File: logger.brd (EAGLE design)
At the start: 99 x 44.1 mm, 78 parts, among them IC1 LTC4412, J1 POWER_JACKPTH, Q1 FDN360P, Q2 FDN360P, Q3 2N7002PW, Q4 2N7002PW, U1 DS3231MZ/V+T, U2 FT231X-Q

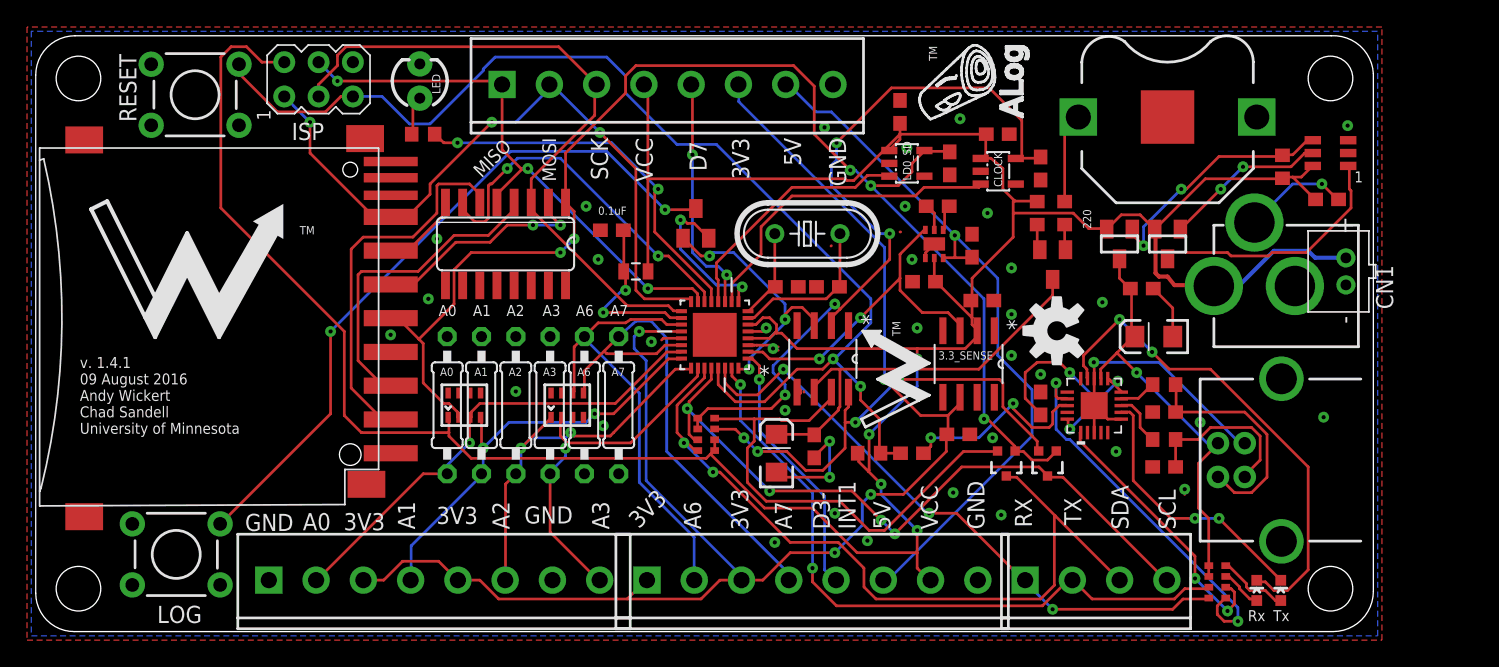
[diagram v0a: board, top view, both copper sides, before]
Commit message: change 3V3 power supply with jumpers, routing needs finishing
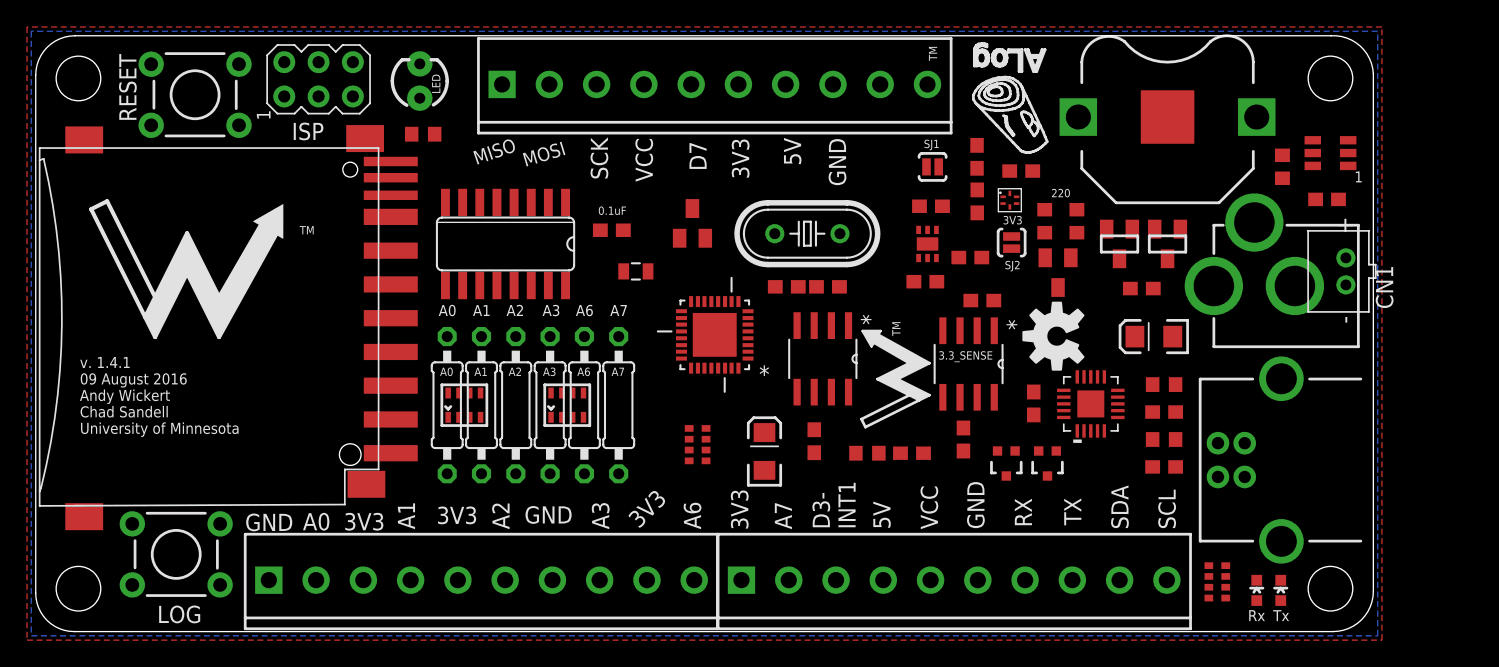
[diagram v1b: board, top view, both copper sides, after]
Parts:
- removed CLOCK, LD0_SD: LP2985, adafruit:SOT23-5L
- removed CLOCK_CIN, SD_CIN: 1uF, rcl:C0603
- removed C_LDO_CLOCK, C_LDO_SD: 2.2uF, resistor:C0603
- removed JP6: (no value), SparkFun-Connectors:SCREWTERMINAL-3.5MM-4
- added 3V3: (no value), csandell:6-TMLF
- added CLOCK_CIN1, CLOCK_CIN2, CLOCK_CIN3: 1uF, rcl:C0603
- added SJ1, SJ2: SOLDERJUMPERNO, SparkFun-Retired:SJ_2S-NO
- 5V_CHARGE_PUMP: value TPS60150 -> 5V5
- D2: value BAT54C -> BAT54
- H0, H1, H3: device SparkFun:SCREWTERMINAL-3.5MM-8 -> SparkFun-Connectors:SCREWTERMINAL-3.5MM-8
- moved H1 7.00 mm to (52.3, 3.81)
- moved U$2 4.47 mm to (72.1, 38.3), turned to 180 degrees
- moved RCLK2 1.09 mm to (77.1, 30.4)
- moved RN2 0.99 mm to (49.0, 13.8)
- moved CLOCK_BATT_DECOUPLE 0.90 mm to (54.0, 13.3)
- moved C_BOOST_3 0.89 mm to (69.2, 27.7), turned to 180 degrees
- moved RCKL1 0.82 mm to (74.7, 30.4)
- moved D1 0.72 mm to (75.7, 26.6)
- moved C_LDO_SENSE 0.54 mm to (68.7, 14.2), turned to 90 degrees
- moved C1 0.51 mm to (73.9, 16.9)
- moved 5V_CHARGE_PUMP 0.50 mm to (66.0, 28.7)
- moved C_BOOST_2 0.50 mm to (66.3, 31.5)
- moved LOGO1 0.40 mm to (75.6, 21.9)
- moved CLOCK_BATT_DECOUP 0.38 mm to (57.7, 14.1)
- moved U2 0.28 mm to (78.1, 16.9)
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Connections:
- removed net D6-CLOCK_3V3_SWITCH: CLOCK.3, MCU.10
- removed net D8-SD_3V3_SWITCH: LD0_SD.3, MCU.12
- new net D6-CLOCK_SD_SWITCH: 3V3.3, MCU.10
- new net D8-EXT: H3.7, MCU.12
- new net N$19: 3V3.4, SJ2.2
- new net N$20: 3V3.1, CLOCK_CIN2.1, SJ1.2
- net +3V3: now also H0.9, H3.8, SJ1.1; no longer H1.3, H3.6
- net 5V: now also H1.4, H3.9; no longer H1.6, H3.7
- net A6: now also H0.10; no longer H1.2
- net A7: now also H1.2; no longer H1.4
- net CLK: now also H3.4; no longer H3.3
- net D3-INT1: now also H1.3; no longer H1.5
- net D4-SENSE_LDO_SWITCH: now also SJ2.1
- net D7-CS-EXT: now also H3.6; no longer H3.5
- net DI: now also H3.2; no longer H3.1
- net DO: now also H3.3; no longer H3.2
- net GND: now also 3V3.5, CLOCK_CIN1.2, CLOCK_CIN2.2, CLOCK_CIN3.2, H1.6, H3.1, H3.10; no longer CLOCK.2, CLOCK_CIN.2, C_LDO_CLOCK.1, C_LDO_SD.1, H1.8, H3.8, LD0_SD.2, SD_CIN.2
- net RX-I: now also H1.7; no longer JP6.1
- net SCL: now also H1.10; no longer JP6.4
- net SDA: now also H1.9; no longer JP6.3
- net TX-O: now also H1.8; no longer JP6.2
- net VCC: now also 3V3.6, CLOCK_CIN1.1, H1.5, H3.5; no longer CLOCK.1, CLOCK_CIN.1, H1.7, H3.4, LD0_SD.1, SD_CIN.1
- net VCL: no longer CLOCK.5, C_LDO_CLOCK.2
- net VDD: now also 3V3.2, CLOCK_CIN3.1; no longer C_LDO_SD.2, LD0_SD.5
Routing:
- net VCC: track 244.3 -> 0.00 mm, vias 4 -> 0
- net +3V3: track 114.1 -> 0.00 mm, vias 4 -> 0
- net VDD: track 99.7 -> 0.00 mm, vias 5 -> 0
- net RESET: track 87.5 -> 0.00 mm, vias 2 -> 0
- net SDA: track 58.2 -> 0.00 mm, vias 2 -> 0
- net VCL: track 56.8 -> 0.00 mm, vias 4 -> 0
- net GND: track 56.5 -> 0.00 mm, vias 38 -> 0
- net 5V: track 53.6 -> 0.00 mm, vias 1 -> 0
- net N$11: track 52.1 -> 0.00 mm, vias 2 -> 0
- net DO: track 52.1 -> 0.00 mm, vias 3 -> 0
- net SCL: track 51.5 -> 0.00 mm, vias 4 -> 0
- net TX-O: track 50.2 -> 0.00 mm, vias 2 -> 0
- net CLK: track 49.8 -> 0.00 mm
- net RX-I: track 46.1 -> 0.00 mm, vias 3 -> 0
- net DI: track 41.9 -> 0.00 mm, vias 3 -> 0
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
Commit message: Routed and ready for Wickert check of approval
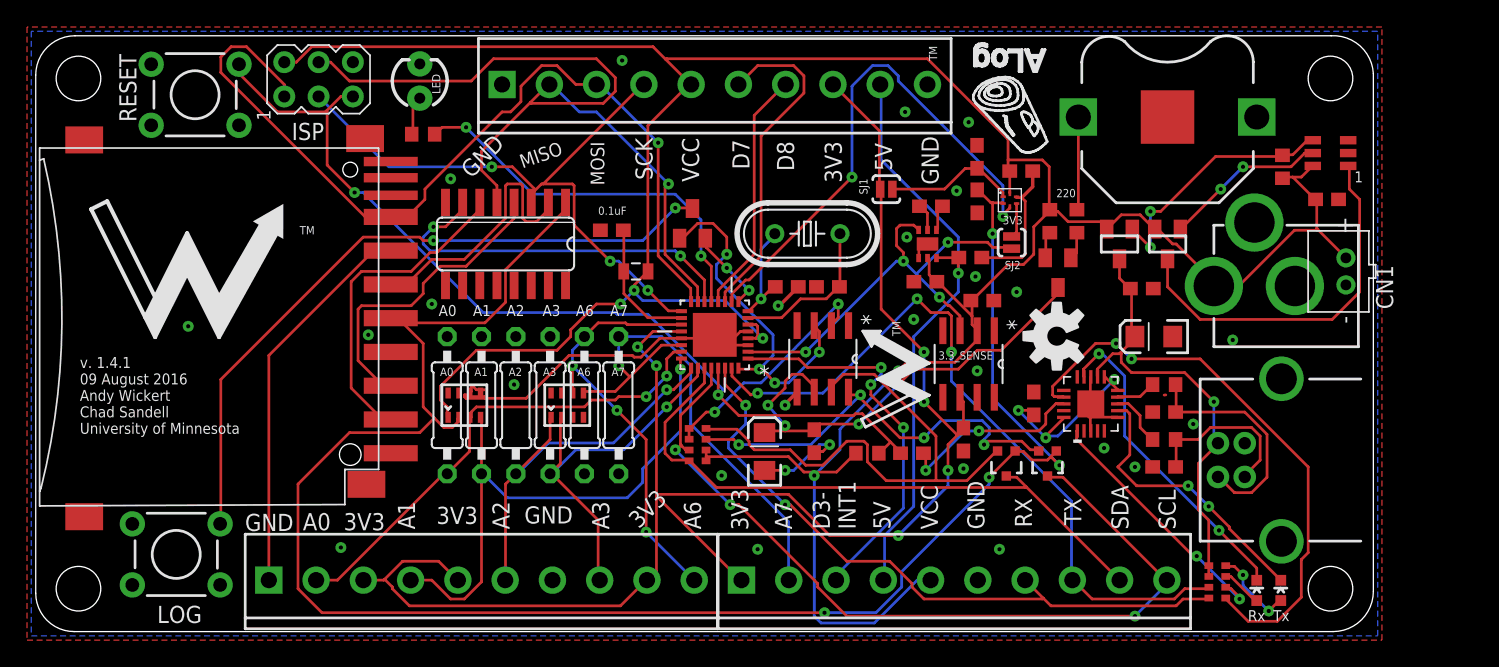
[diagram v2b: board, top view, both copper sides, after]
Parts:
- moved SJ1 3.81 mm to (63.0, 32.8)
- moved RCKL1 0.38 mm to (75.1, 30.4)
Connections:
- net GND: now also MCU.33
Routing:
- net VCC: track 0.00 -> 227.4 mm, vias 0 -> 5
- net VDD: track 0.00 -> 138.0 mm, vias 0 -> 4
- net +3V3: track 0.00 -> 121.4 mm, vias 0 -> 6
- net GND: track 0.00 -> 92.1 mm, vias 0 -> 28
- net RESET: track 0.00 -> 70.3 mm, vias 0 -> 2
- net DO: track 0.00 -> 65.9 mm, vias 0 -> 1
- net DI: track 0.00 -> 64.5 mm, vias 0 -> 1
- net SCL: track 0.00 -> 63.1 mm, vias 0 -> 3
- net TX-O: track 0.00 -> 55.3 mm, vias 0 -> 3
- net N$11: track 0.00 -> 51.2 mm, vias 0 -> 2
- net RX-I: track 0.00 -> 49.9 mm, vias 0 -> 2
- net CLK: track 0.00 -> 48.0 mm, vias 0 -> 3
- net SDA: track 0.00 -> 47.0 mm
- net 5V: track 0.00 -> 44.3 mm, vias 0 -> 1
- net N$27: track 0.00 -> 42.5 mm, vias 0 -> 2
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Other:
- board text added: "D8"

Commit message: Added version number
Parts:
- moved U$2 0.52 mm to (72.6, 38.5)
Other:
- board text added: "v. 2.0 beta 29 October 2016 Andy Wickert Chad Sandell University of Minnesota"
- board text added: "v2.0b"
- board text removed: "v. 1.4.1 09 August 2016 Andy Wickert Chad Sandell University of Minnesota"
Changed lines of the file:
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@@
 <text x="70.2626" y="7.5702" size="1.27" layer="21" rot="R90">GND</text>
 <text x="66.8175" y="7.5702" size="1.27" layer="21" rot="R90">VCC</text>
-<text x="3.2766" y="14.6431" size="0.8128" layer="21">v. 1.4.1
-09 August 2016
+<text x="3.2766" y="14.6431" size="0.8128" layer="21">v. 2.0 beta
+29 October 2016
 Andy Wickert
 Chad Sandell
@@
 <text x="38.7802" y="36.3083" size="1.016" layer="21" rot="R199">MISO</text>
 <text x="54.8965" y="36.3083" size="1.27" layer="21" rot="R270">D8</text>
+<text x="69.469" y="40.513" size="0.8128" layer="21" rot="R90">v2.0b</text>
 </plain>
 <attributes>
@@
 </element>
 <element name="JP1" library="SparkFun" package="STAND-OFF" value="STAND-OFF" x="3.175" y="3.175" smashed="yes"/>
-<element name="U$2" library="awickert" package="ALOG_LOGO_V1_SMALL" value="ALOG_LOGO_V1_5.5MM" x="72.084" y="38.342" smashed="yes" rot="R180"/>
+<element name="U$2" library="awickert" package="ALOG_LOGO_V1_SMALL" value="ALOG_LOGO_V1_5.5MM" x="72.592" y="38.469" smashed="yes" rot="R180"/>
 <element name="JP4" library="SparkFun" package="STAND-OFF" value="STAND-OFF" x="3.175" y="40.9575" smashed="yes"/>
 <element name="A1" library="resistor" package="0207/10" value="" x="33.02" y="16.764" smashed="yes" rot="R270">
@@
 <via x="69.088" y="37.719" extent="1-16" drill="0.3048" shape="octagon"/>
 <via x="64.389" y="38.481" extent="1-16" drill="0.3048" shape="octagon"/>
-<wire x1="49.657" y1="22.86" x2="49.657" y2="22.86" width="0" layer="19" extent="1-16"/>
 <wire x1="49.657" y1="22.86" x2="50.292" y2="22.225" width="0.254" layer="1"/>
 <wire x1="50.292" y1="22.225" x2="50.292" y2="21.971" width="0.254" layer="1"/>
